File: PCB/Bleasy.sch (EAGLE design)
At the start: 14 parts, among them IC1 ATMEGA328-PU, Q1 8 MHz

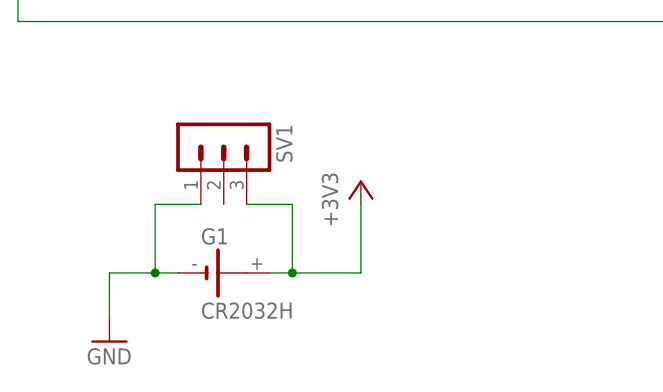
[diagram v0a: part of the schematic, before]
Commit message: New cell coin adapter
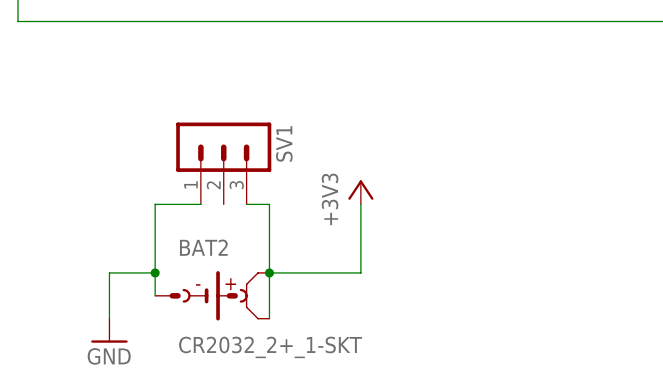
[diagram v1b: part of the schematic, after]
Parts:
- removed G1: CR2032H, battery:CR2032H
- added BAT2: CR2032_2+_1-SKT, con_bat_2032__s_:CR2032_2+_1-SKT
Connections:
- net +3V3: now also BAT2.POS1, BAT2.POS2; no longer G1.+
- net GND: now also BAT2.NEG; no longer G1.-
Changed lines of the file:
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@@
 <setting verticaltext="up"/>
 </settings>
-<grid distance="0.1" unitdist="inch" unit="inch" style="lines" multiple="1" display="yes" altdistance="0.01" altunitdist="inch" altunit="inch"/>
+<grid distance="0.1" unitdist="inch" unit="inch" style="lines" multiple="1" display="no" altdistance="0.01" altunitdist="inch" altunit="inch"/>
 <layers>
 <layer number="1" name="Top" color="4" fill="1" visible="no" active="no"/>
@@
 <part name="GND6" library="supply1" deviceset="GND" device=""/>
 <part name="LED1" library="led" deviceset="LED" device="3MM"/>
-<part name="G1" library="battery" deviceset="CR2032H" device=""/>
 <part name="GND7" library="supply1" deviceset="GND" device=""/>
 <part name="+3V5" library="supply1" deviceset="+3V3" device=""/>
@@
 <part name="ADIO" library="con-lstb" deviceset="MA06-2" device=""/>
 <part name="GND8" library="supply1" deviceset="GND" device=""/>
+<part name="BAT2" library="con_bat_2032__s_" deviceset="CR2032_2+_1-" device="SKT"/>
 </parts>
 <sheets>
@@
 <instance part="GND6" gate="1" x="198.12" y="78.74"/>
 <instance part="LED1" gate="G$1" x="198.12" y="86.36"/>
-<instance part="G1" gate="1" x="10.16" y="35.56"/>
 <instance part="GND7" gate="1" x="-2.54" y="27.94"/>
 <instance part="+3V5" gate="G$1" x="25.4" y="45.72"/>
@@
 <instance part="ADIO" gate="1" x="96.52" y="127"/>
 <instance part="GND8" gate="1" x="104.14" y="114.3"/>
+<instance part="BAT2" gate="B1" x="10.16" y="33.02"/>
 </instances>
 <busses>
@@
 <pinref part="LED1" gate="G$1" pin="C"/>
 <pinref part="GND6" gate="1" pin="GND"/>
-</segment>
-<segment>
-<pinref part="G1" gate="1" pin="-"/>
-<wire x1="5.08" y1="35.56" x2="2.54" y2="35.56" width="0.1524" layer="91"/>
-<pinref part="GND7" gate="1" pin="GND"/>
-<wire x1="2.54" y1="35.56" x2="-2.54" y2="35.56" width="0.1524" layer="91"/>
-<wire x1="-2.54" y1="35.56" x2="-2.54" y2="30.48" width="0.1524" layer="91"/>
-<pinref part="SV1" gate="G$1" pin="1"/>
-<wire x1="7.62" y1="43.18" x2="2.54" y2="43.18" width="0.1524" layer="91"/>
-<wire x1="2.54" y1="43.18" x2="2.54" y2="35.56" width="0.1524" layer="91"/>
-<junction x="2.54" y="35.56"/>
 </segment>
 <segment>
@@
 <pinref part="UART" gate="1" pin="2"/>
 </segment>
+<segment>
+<pinref part="GND7" gate="1" pin="GND"/>
+<wire x1="-2.54" y1="30.48" x2="-2.54" y2="35.56" width="0.1524" layer="91"/>
+<wire x1="-2.54" y1="35.56" x2="2.54" y2="35.56" width="0.1524" layer="91"/>
+<pinref part="SV1" gate="G$1" pin="1"/>
+<wire x1="7.62" y1="43.18" x2="2.54" y2="43.18" width="0.1524" layer="91"/>
+<wire x1="2.54" y1="43.18" x2="2.54" y2="35.56" width="0.1524" layer="91"/>
+<pinref part="BAT2" gate="B1" pin="NEG"/>
+<wire x1="2.54" y1="33.02" x2="2.54" y2="35.56" width="0.1524" layer="91"/>
+<junction x="2.54" y="35.56"/>
+</segment>
 </net>
 <net name="+3V3" class="0">
@@
 </segment>
 <segment>
-<pinref part="G1" gate="1" pin="+"/>
-<wire x1="15.24" y1="35.56" x2="17.78" y2="35.56" width="0.1524" layer="91"/>
-<pinref part="+3V5" gate="G$1" pin="+3V3"/>
-<wire x1="17.78" y1="35.56" x2="25.4" y2="35.56" width="0.1524" layer="91"/>
-<wire x1="25.4" y1="35.56" x2="25.4" y2="43.18" width="0.1524" layer="91"/>
-<pinref part="SV1" gate="G$1" pin="3"/>
-<wire x1="12.7" y1="43.18" x2="17.78" y2="43.18" width="0.1524" layer="91"/>
-<wire x1="17.78" y1="43.18" x2="17.78" y2="35.56" width="0.1524" layer="91"/>
-<junction x="17.78" y="35.56"/>
-</segment>
-<segment>
 <pinref part="+3V3" gate="G$1" pin="+3V3"/>
 <wire x1="109.22" y1="149.86" x2="109.22" y2="147.32" width="0.1524" layer="91"/>
@@
 <wire x1="109.22" y1="147.32" x2="121.92" y2="147.32" width="0.1524" layer="91"/>
 </segment>
-</net>
+<segment>
+<pinref part="+3V5" gate="G$1" pin="+3V3"/>
+<wire x1="15.24" y1="35.56" x2="25.4" y2="35.56" width="0.1524" layer="91"/>
+<wire x1="25.4" y1="35.56" x2="25.4" y2="43.18" width="0.1524" layer="91"/>
+<pinref part="SV1" gate="G$1" pin="3"/>
+<wire x1="12.7" y1="43.18" x2="15.24" y2="43.18" width="0.1524" layer="91"/>
+<wire x1="15.24" y1="43.18" x2="15.24" y2="35.56" width="0.1524" layer="91"/>
+<pinref part="BAT2" gate="B1" pin="POS1"/>
+<junction x="15.24" y="35.56"/>
+<pinref part="BAT2" gate="B1" pin="POS2"/>
+<wire x1="15.24" y1="30.48" x2="15.24" y2="35.56" width="0.1524" layer="91"/>
+</segment>
+</net>
